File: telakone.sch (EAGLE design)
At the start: 171 parts, among them X10 MPT0.5/8-2.54, X11 MPT0.5/8-2.54, X2 MPT0.5/8-2.54, X3 MPT0.5/8-2.54, X4 PIIKKIRIMA-2, X5 PIIKKIRIMA-5, X7 U.FL-R-SMT-1, X8 MPT0.5/8-2.54, X9 629105136821

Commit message: placement, all on board
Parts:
- added C48, C49, C52: (no value), omat_ic_2:CAP0603
- added Y1, Y2, Y3, Y4: PTH2.6-5.5SQ, EKE:PTH2.6-5.5SQ
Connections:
- net +3V3: now also C48.1, C49.1, C52.1
- net GND: now also C48.2, C49.2, C52.2
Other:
- note added: "MOUNTING HOLES"
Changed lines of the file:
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@@
 <part name="V27" library="omat_ic_2" deviceset="ESDAXXSC6" device="" value="ESDAXXSC6"/>
 <part name="GND71" library="EKE" deviceset="GND" device=""/>
+<part name="Y1" library="EKE" deviceset="PTH" device="2.6-5.5SQ"/>
+<part name="Y2" library="EKE" deviceset="PTH" device="2.6-5.5SQ"/>
+<part name="Y3" library="EKE" deviceset="PTH" device="2.6-5.5SQ"/>
+<part name="Y4" library="EKE" deviceset="PTH" device="2.6-5.5SQ"/>
+<part name="C48" library="omat_ic_2" deviceset="CAP" device="0603"/>
+<part name="+3V41" library="EKE" deviceset="+3V3" device=""/>
+<part name="GND72" library="EKE" deviceset="GND" device=""/>
+<part name="C49" library="omat_ic_2" deviceset="CAP" device="0603"/>
+<part name="+3V44" library="EKE" deviceset="+3V3" device=""/>
+<part name="GND75" library="EKE" deviceset="GND" device=""/>
+<part name="C52" library="omat_ic_2" deviceset="CAP" device="0603"/>
+<part name="+3V45" library="EKE" deviceset="+3V3" device=""/>
+<part name="GND76" library="EKE" deviceset="GND" device=""/>
 </parts>
 <sheets>
@@
 <description>POWER</description>
 <plain>
+<text x="93.98" y="66.04" size="1.778" layer="97">MOUNTING HOLES</text>
 </plain>
 <instances>
@@
 <instance part="F1" gate="G$1" x="111.76" y="177.8" rot="MR0"/>
 <instance part="V16" gate="G$1" x="121.92" y="167.64" rot="R90"/>
+<instance part="Y1" gate="G$1" x="106.68" y="55.88"/>
+<instance part="Y2" gate="G$1" x="106.68" y="45.72"/>
+<instance part="Y3" gate="G$1" x="106.68" y="35.56"/>
+<instance part="Y4" gate="G$1" x="106.68" y="25.4"/>
 </instances>
 <busses>
@@
 <instance part="V27" gate="G$1" x="309.88" y="76.2"/>
 <instance part="GND71" gate="1" x="292.1" y="63.5"/>
+<instance part="C48" gate="G$1" x="152.4" y="147.32"/>
+<instance part="+3V41" gate="G$1" x="152.4" y="152.4"/>
+<instance part="GND72" gate="1" x="152.4" y="139.7"/>
+<instance part="C49" gate="G$1" x="213.36" y="40.64"/>
+<instance part="+3V44" gate="G$1" x="213.36" y="45.72"/>
+<instance part="GND75" gate="1" x="213.36" y="33.02"/>
+<instance part="C52" gate="G$1" x="104.14" y="175.26"/>
+<instance part="+3V45" gate="G$1" x="104.14" y="180.34"/>
+<instance part="GND76" gate="1" x="104.14" y="167.64"/>
 </instances>
 <busses>
@@
 <junction x="292.1" y="73.66"/>
 </segment>
+<segment>
+<pinref part="C48" gate="G$1" pin="2"/>
+<pinref part="GND72" gate="1" pin="GND"/>
+</segment>
+<segment>
+<pinref part="C49" gate="G$1" pin="2"/>
+<pinref part="GND75" gate="1" pin="GND"/>
+</segment>
+<segment>
+<pinref part="C52" gate="G$1" pin="2"/>
+<pinref part="GND76" gate="1" pin="GND"/>
+</segment>
 </net>
 <net name="+3V3" class="0">
@@
 <wire x1="203.2" y1="66.04" x2="203.2" y2="71.12" width="0.1524" layer="91"/>
 </segment>
-</net>
+<segment>
+<pinref part="C48" gate="G$1" pin="1"/>
+<pinref part="+3V41" gate="G$1" pin="+3V3"/>
+</segment>
+<segment>
+<pinref part="C49" gate="G$1" pin="1"/>
+<pinref part="+3V44" gate="G$1" pin="+3V3"/>
+</segment>
+<segment>
+<pinref part="C52" gate="G$1" pin="1"/>
+<pinref part="+3V45" gate="G$1" pin="+3V3"/>
+</segment>
+</net>

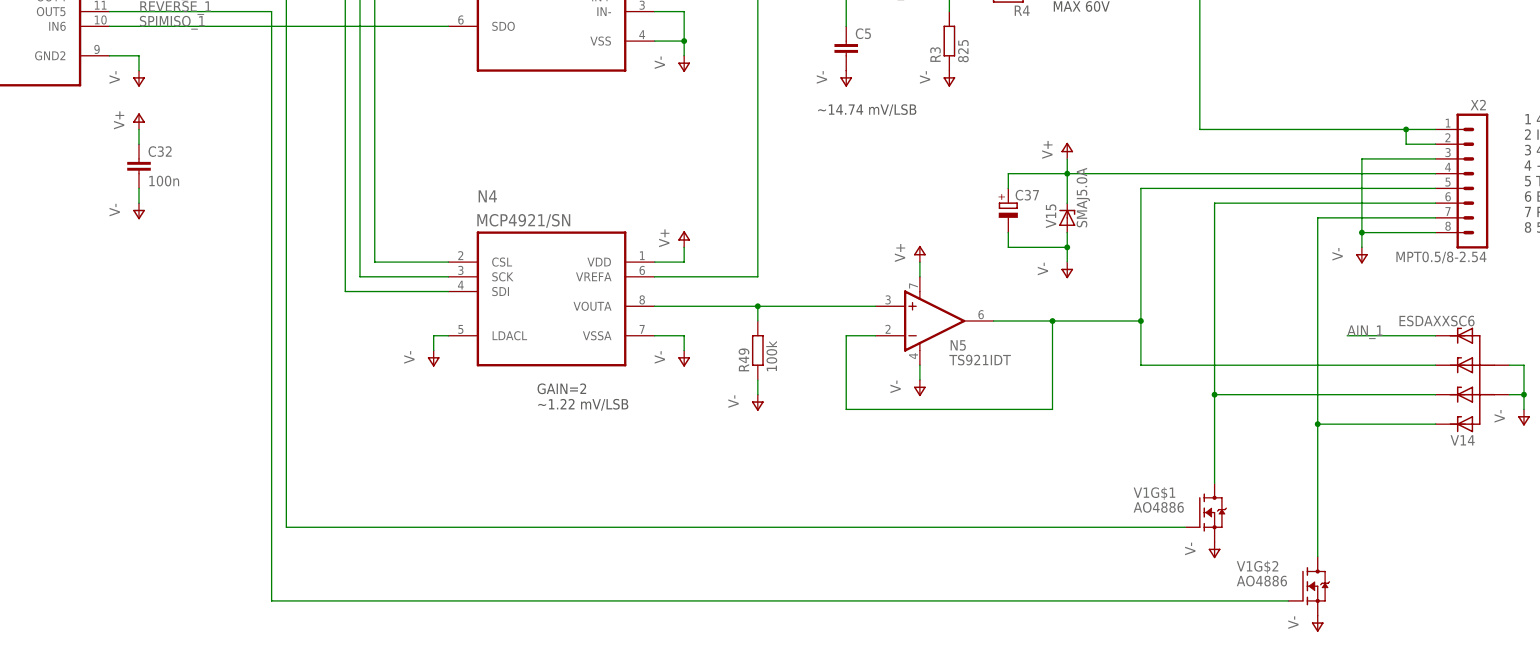
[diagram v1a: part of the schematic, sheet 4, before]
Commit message: isolation groups routed
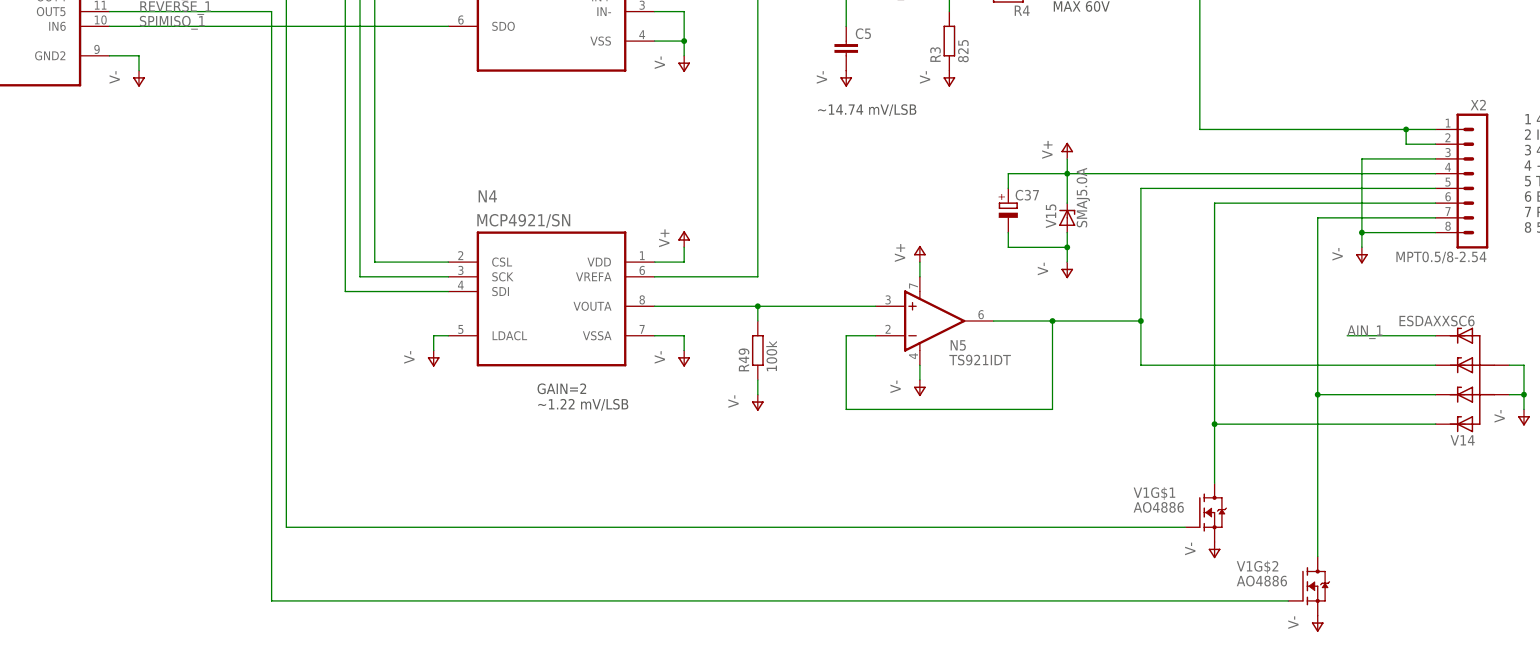
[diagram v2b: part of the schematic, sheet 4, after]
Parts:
- removed C32, C40: 100n, omat_ic_2:CAP0603
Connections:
- net BRAKE_OD_1: now also V14.C; no longer V14.C1
- net BRAKE_OD_2: now also V25.C; no longer V25.C1
- net REVERSE_OD_1: now also V14.C1; no longer V14.C
- net REVERSE_OD_2: now also V25.C1; no longer V25.C
- net V+1: no longer C32.1
- net V+2: no longer C40.1
- net V-1: no longer C32.2
- net V-2: no longer C40.2
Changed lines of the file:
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@@
 <part name="GND56" library="EKE" deviceset="GND" device=""/>
 <part name="+3V34" library="EKE" deviceset="+3V3" device=""/>
-<part name="C32" library="omat_ic_2" deviceset="CAP" device="0603" value="100n"/>
-<part name="P-16" library="EKE" deviceset="V-" device=""/>
-<part name="P+13" library="EKE" deviceset="V+" device=""/>
 <part name="C33" library="omat_ic_2" deviceset="CAP" device="0603" value="100n"/>
 <part name="P-17" library="EKE" deviceset="V-" device=""/>
@@
 <part name="GND57" library="EKE" deviceset="GND" device=""/>
 <part name="FRAME8" library="omat_ic_2" deviceset="DINA3_L" device=""/>
-<part name="C40" library="omat_ic_2" deviceset="CAP" device="0603" value="100n"/>
-<part name="P-36" library="EKE" deviceset="V-" device=""/>
-<part name="P+27" library="EKE" deviceset="V+" device=""/>
 <part name="C41" library="omat_ic_2" deviceset="CAP" device="0603" value="100n"/>
 <part name="P-37" library="EKE" deviceset="V-" device=""/>
@@
 <instance part="FRAME2" gate="G$1" x="0" y="0"/>
 <instance part="FRAME2" gate="G$2" x="287.02" y="0"/>
-<instance part="C32" gate="G$1" x="78.74" y="119.38"/>
-<instance part="P-16" gate="1" x="78.74" y="109.22"/>
-<instance part="P+13" gate="1" x="78.74" y="127"/>
 <instance part="C33" gate="G$1" x="203.2" y="187.96"/>
 <instance part="P-17" gate="1" x="203.2" y="177.8"/>
@@
 <pinref part="V1" gate="G$1" pin="D"/>
 <wire x1="302.26" y1="111.76" x2="264.16" y2="111.76" width="0.1524" layer="91"/>
-<wire x1="264.16" y1="111.76" x2="264.16" y2="78.74" width="0.1524" layer="91"/>
-<pinref part="V14" gate="G$1" pin="C1"/>
-<wire x1="264.16" y1="78.74" x2="264.16" y2="63.5" width="0.1524" layer="91"/>
-<wire x1="302.26" y1="78.74" x2="264.16" y2="78.74" width="0.1524" layer="91"/>
-<junction x="264.16" y="78.74"/>
+<wire x1="264.16" y1="111.76" x2="264.16" y2="73.66" width="0.1524" layer="91"/>
+<pinref part="V14" gate="G$1" pin="C"/>
+<wire x1="264.16" y1="73.66" x2="264.16" y2="63.5" width="0.1524" layer="91"/>
+<wire x1="302.26" y1="73.66" x2="264.16" y2="73.66" width="0.1524" layer="91"/>
+<junction x="264.16" y="73.66"/>
 </segment>
 </net>
@@
 <pinref part="V1" gate="G$2" pin="D"/>
 <wire x1="302.26" y1="109.22" x2="281.94" y2="109.22" width="0.1524" layer="91"/>
-<wire x1="281.94" y1="109.22" x2="281.94" y2="73.66" width="0.1524" layer="91"/>
-<pinref part="V14" gate="G$1" pin="C"/>
-<wire x1="281.94" y1="73.66" x2="281.94" y2="50.8" width="0.1524" layer="91"/>
-<wire x1="302.26" y1="73.66" x2="281.94" y2="73.66" width="0.1524" layer="91"/>
-<junction x="281.94" y="73.66"/>
+<wire x1="281.94" y1="109.22" x2="281.94" y2="78.74" width="0.1524" layer="91"/>
+<pinref part="V14" gate="G$1" pin="C1"/>
+<wire x1="281.94" y1="78.74" x2="281.94" y2="50.8" width="0.1524" layer="91"/>
+<wire x1="302.26" y1="78.74" x2="281.94" y2="78.74" width="0.1524" layer="91"/>
+<junction x="281.94" y="78.74"/>
 </segment>
 </net>
@@
 <wire x1="73.66" y1="160.02" x2="78.74" y2="160.02" width="0.1524" layer="91"/>
 <wire x1="78.74" y1="160.02" x2="78.74" y2="162.56" width="0.1524" layer="91"/>
-</segment>
-<segment>
-<pinref part="C32" gate="G$1" pin="1"/>
-<pinref part="P+13" gate="1" pin="V+"/>
-<wire x1="78.74" y1="121.92" x2="78.74" y2="124.46" width="0.1524" layer="91"/>
 </segment>
 <segment>
@@
 <wire x1="73.66" y1="137.16" x2="78.74" y2="137.16" width="0.1524" layer="91"/>
 <wire x1="78.74" y1="137.16" x2="78.74" y2="134.62" width="0.1524" layer="91"/>
-</segment>
-<segment>
-<pinref part="C32" gate="G$1" pin="2"/>
-<pinref part="P-16" gate="1" pin="V-"/>
-<wire x1="78.74" y1="111.76" x2="78.74" y2="114.3" width="0.1524" layer="91"/>
 </segment>
 <segment>
@@
 <instance part="FRAME8" gate="G$1" x="0" y="0"/>
 <instance part="FRAME8" gate="G$2" x="287.02" y="0"/>
-<instance part="C40" gate="G$1" x="78.74" y="119.38"/>
-<instance part="P-36" gate="1" x="78.74" y="109.22"/>
-<instance part="P+27" gate="1" x="78.74" y="127"/>
 <instance part="C41" gate="G$1" x="203.2" y="187.96"/>
 <instance part="P-37" gate="1" x="203.2" y="177.8"/>
@@
 <pinref part="V6" gate="G$1" pin="D"/>
 <wire x1="302.26" y1="111.76" x2="264.16" y2="111.76" width="0.1524" layer="91"/>
-<wire x1="264.16" y1="111.76" x2="264.16" y2="78.74" width="0.1524" layer="91"/>
-<pinref part="V25" gate="G$1" pin="C1"/>
-<wire x1="264.16" y1="78.74" x2="264.16" y2="63.5" width="0.1524" layer="91"/>
-<wire x1="302.26" y1="78.74" x2="264.16" y2="78.74" width="0.1524" layer="91"/>
-<junction x="264.16" y="78.74"/>
+<wire x1="264.16" y1="111.76" x2="264.16" y2="73.66" width="0.1524" layer="91"/>
+<pinref part="V25" gate="G$1" pin="C"/>
+<wire x1="264.16" y1="73.66" x2="264.16" y2="63.5" width="0.1524" layer="91"/>
+<wire x1="302.26" y1="73.66" x2="264.16" y2="73.66" width="0.1524" layer="91"/>
+<junction x="264.16" y="73.66"/>
 </segment>
 </net>
@@
 <pinref part="V6" gate="G$2" pin="D"/>
 <wire x1="302.26" y1="109.22" x2="281.94" y2="109.22" width="0.1524" layer="91"/>
-<wire x1="281.94" y1="109.22" x2="281.94" y2="73.66" width="0.1524" layer="91"/>
-<pinref part="V25" gate="G$1" pin="C"/>
-<wire x1="281.94" y1="73.66" x2="281.94" y2="50.8" width="0.1524" layer="91"/>
-<wire x1="302.26" y1="73.66" x2="281.94" y2="73.66" width="0.1524" layer="91"/>
-<junction x="281.94" y="73.66"/>
+<wire x1="281.94" y1="109.22" x2="281.94" y2="78.74" width="0.1524" layer="91"/>
+<pinref part="V25" gate="G$1" pin="C1"/>
+<wire x1="281.94" y1="78.74" x2="281.94" y2="50.8" width="0.1524" layer="91"/>
+<wire x1="302.26" y1="78.74" x2="281.94" y2="78.74" width="0.1524" layer="91"/>
+<junction x="281.94" y="78.74"/>
 </segment>
 </net>
@@
 <wire x1="73.66" y1="160.02" x2="78.74" y2="160.02" width="0.1524" layer="91"/>
 <wire x1="78.74" y1="160.02" x2="78.74" y2="162.56" width="0.1524" layer="91"/>
-</segment>
-<segment>
-<pinref part="C40" gate="G$1" pin="1"/>
-<pinref part="P+27" gate="1" pin="V+"/>
-<wire x1="78.74" y1="121.92" x2="78.74" y2="124.46" width="0.1524" layer="91"/>
 </segment>
 <segment>
@@
 <net name="V-2" class="0">
 <segment>
-<pinref part="C40" gate="G$1" pin="2"/>
-<pinref part="P-36" gate="1" pin="V-"/>
-<wire x1="78.74" y1="111.76" x2="78.74" y2="114.3" width="0.1524" layer="91"/>
-</segment>
-<segment>
 <pinref part="C41" gate="G$1" pin="2"/>

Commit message: work commit, routing in progress
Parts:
- added C32, C40, C53: (no value), omat_ic_2:CAP0805
- added V28: WURTH 82402304, omat_ic_2:ESDAXXSC6
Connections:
- net N$33 renamed PA11-USBD-
- net N$36 renamed PA12-USBD+
- net N$37 renamed USBD+
- net N$38 renamed USBD-
- net N$39 renamed PA9-USBVBUS
- net N$40 renamed USBVBUS
- net N$41 renamed PA10-USBID-PULLUP
- net +12V: now also C32.1, C40.1, C53.1
- net BUTTON1: now also V26.C1; no longer V26.C
- net BUTTON2: now also V26.C2; no longer V26.C1
- net GND: now also C32.2, C40.2, C53.2, V28.A, V28.A1, X6.1, Y1.1, Y2.1, Y3.1, Y4.1; no longer X6.2
- net N$8: now also X6.2; no longer X6.1
- net POT_IN_1: now also V28.C1; no longer V26.C2
- net POT_IN_2: now also V28.C3; no longer V26.C3
- net VREF25BUF: now also V28.C2; no longer V27.C
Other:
- moved on the sheet: X6

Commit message: work commit, routing in progress, less than 100 to go :beer:
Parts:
- removed R18, R27: (no value), omat_ic_2:RES0603
- removed R24, R25: 22, omat_ic_2:RES0603
- removed R26: 1k, omat_ic_2:RES0603
- removed X9: 629105136821, omat_ic_2:629105136821
- added C54: 2u2, omat_ic_2:CAP0603
- added C55: 100n, omat_ic_2:CAP0603
- added C56, C57: (no value), omat_ic_2:CAP0603
- added L3: IND0603, omat_ic_2:IND0603
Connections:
- net N$26 renamed OSCIN
- removed net DSPICLK: D15.IN2
- removed net N$27: D1G$1.PH1/OSCOUT, R18.2
- removed net N$28: C24.1, G1.X2, R18.1
- removed net PA10-USBID-PULLUP: D1G$2.PA10, R27.2
- removed net PA11-USBD-: D1G$2.PA11, R24.2
- removed net PA12-USBD+: D1G$2.PA12, R25.2
- removed net PA9-USBVBUS: D1G$2.PA9, R26.2
- removed net USBD+: R25.1, X9.3
- removed net USBD-: R24.1, X9.2
- removed net USBVBUS: R26.1, X9.1
- new net OSCOUT: C24.1, D1G$1.PH1/OSCOUT, G1.X2
- new net VDDAREF: C54.1, C55.1, L3.1, N3.SHDNL, N3.VDD
- net +3V3: now also C56.1, C57.1, L3.2; no longer N3.SHDNL, N3.VDD, R27.1
- net D2SPICLK: now also D15.IN2
- net GND: now also C54.2, C55.2, C56.2, C57.2, X5.4; no longer X5.5, X9.5
- net RESETL: now also X5.5; no longer X5.4
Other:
- moved on the sheet: C12, N3, R17

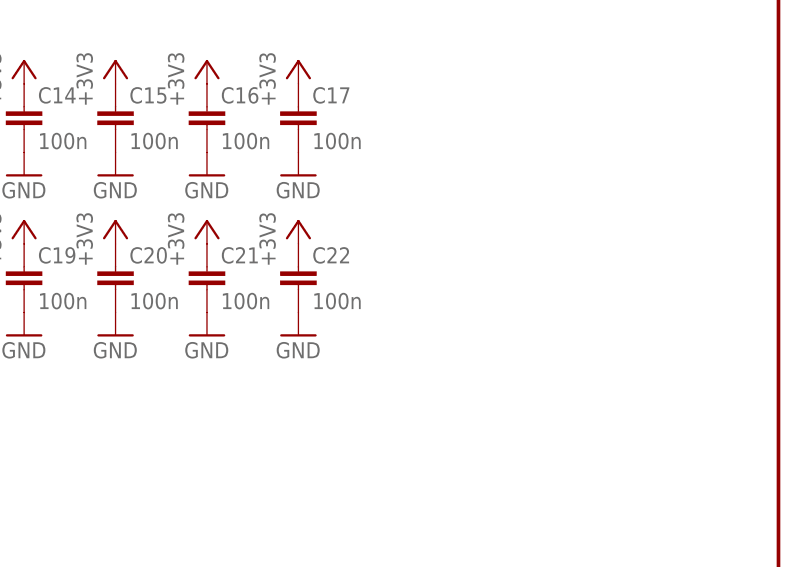
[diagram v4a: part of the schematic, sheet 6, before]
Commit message: fully routed
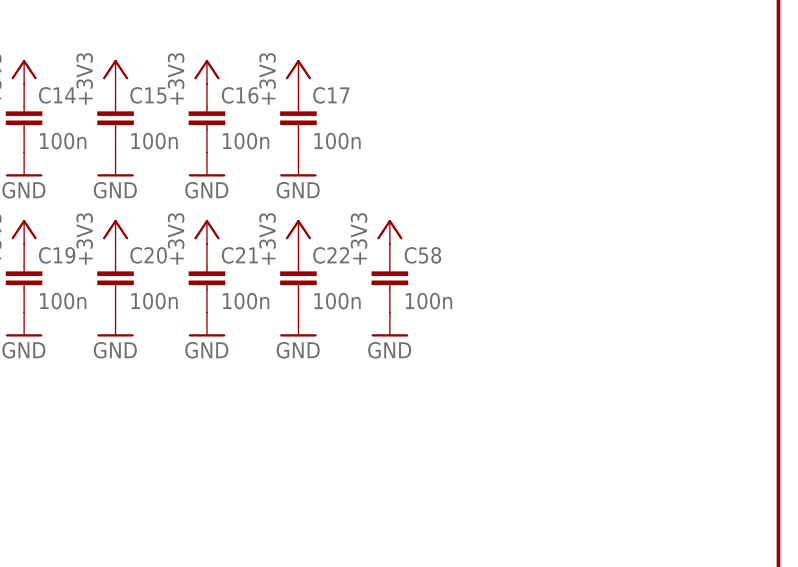
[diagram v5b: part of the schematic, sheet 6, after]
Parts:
- added C58: 100n, omat_ic_2:CAP0603
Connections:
- net +3V3: now also C58.1
- net GND: now also C58.2
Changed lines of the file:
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@@
 <part name="C57" library="omat_ic_2" deviceset="CAP" device="0603"/>
 <part name="GND84" library="EKE" deviceset="GND" device=""/>
+<part name="C58" library="omat_ic_2" deviceset="CAP" device="0603" value="100n"/>
+<part name="GND46" library="EKE" deviceset="GND" device=""/>
+<part name="+3V8" library="EKE" deviceset="+3V3" device=""/>
 </parts>
 <sheets>
@@
 <instance part="GND82" gate="1" x="256.54" y="81.28"/>
 <instance part="+3V7" gate="G$1" x="276.86" y="99.06"/>
+<instance part="C58" gate="G$1" x="345.44" y="167.64"/>
+<instance part="GND46" gate="1" x="345.44" y="160.02"/>
+<instance part="+3V8" gate="G$1" x="345.44" y="172.72"/>
 </instances>
 <busses>
@@
 <pinref part="C54" gate="G$1" pin="2"/>
 <pinref part="GND82" gate="1" pin="GND"/>
+</segment>
+<segment>
+<pinref part="C58" gate="G$1" pin="2"/>
+<pinref part="GND46" gate="1" pin="GND"/>
 </segment>
 </net>
@@
 <wire x1="276.86" y1="93.98" x2="271.78" y2="93.98" width="0.1524" layer="91"/>
 </segment>
-</net>
+<segment>
+<pinref part="C58" gate="G$1" pin="1"/>
+<pinref part="+3V8" gate="G$1" pin="+3V3"/>
+</segment>
+</net>
